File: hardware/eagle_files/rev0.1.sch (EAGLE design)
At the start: 66 parts, among them U1 AD8332ACPZ-R7, U2 AD8333ACPZ-REEL

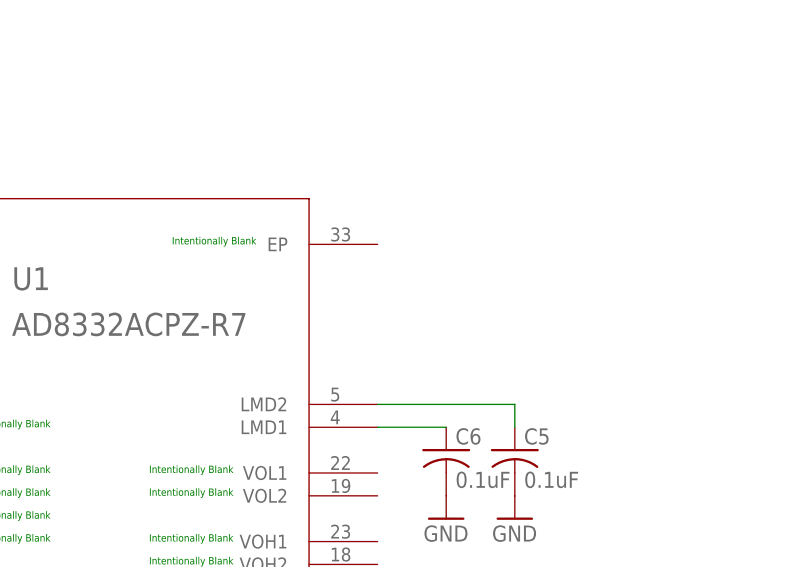
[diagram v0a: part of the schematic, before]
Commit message: Issue 19 fixed: Added all EP to ground plane.
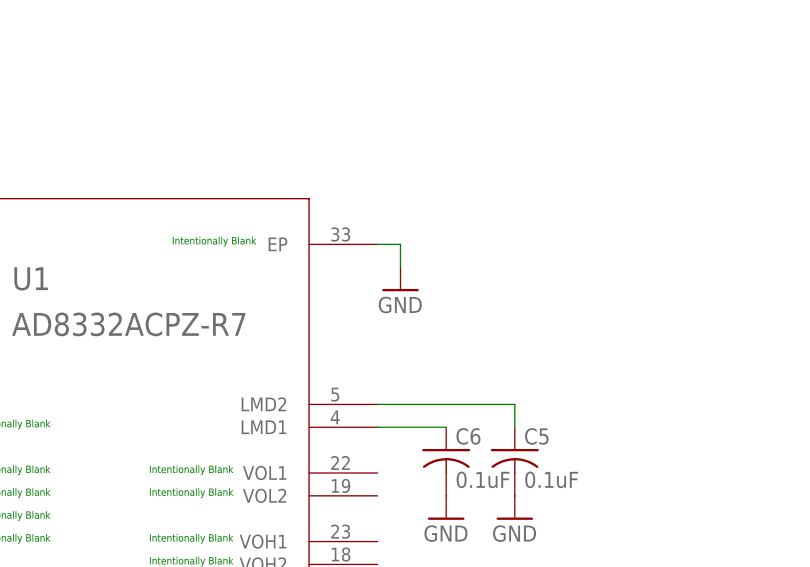
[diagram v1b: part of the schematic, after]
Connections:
- net GND: now also U1.EP
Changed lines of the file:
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@@
 <part name="GND33" library="supply1" deviceset="GND" device=""/>
 <part name="GND34" library="supply1" deviceset="GND" device=""/>
+<part name="GND35" library="supply1" deviceset="GND" device=""/>
 </parts>
 <sheets>
@@
 <instance part="GND33" gate="1" x="-88.9" y="149.86"/>
 <instance part="GND34" gate="1" x="-53.34" y="149.86"/>
+<instance part="GND35" gate="1" x="93.98" y="96.52"/>
 </instances>
 <busses>
@@
 <pinref part="GND34" gate="1" pin="GND"/>
 </segment>
+<segment>
+<pinref part="U1" gate="A" pin="EP"/>
+<pinref part="GND35" gate="1" pin="GND"/>
+<wire x1="91.44" y1="101.6" x2="93.98" y2="101.6" width="0.1524" layer="91"/>
+<wire x1="93.98" y1="101.6" x2="93.98" y2="99.06" width="0.1524" layer="91"/>
+</segment>
 </net>
